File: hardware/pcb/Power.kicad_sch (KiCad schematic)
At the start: 17 parts, among them J4 USB_B_Micro, SW2 CSS-1210TB, U3 MCP73831-2-OT, U4 TL431DBZ, U5 TLV73333PDBV

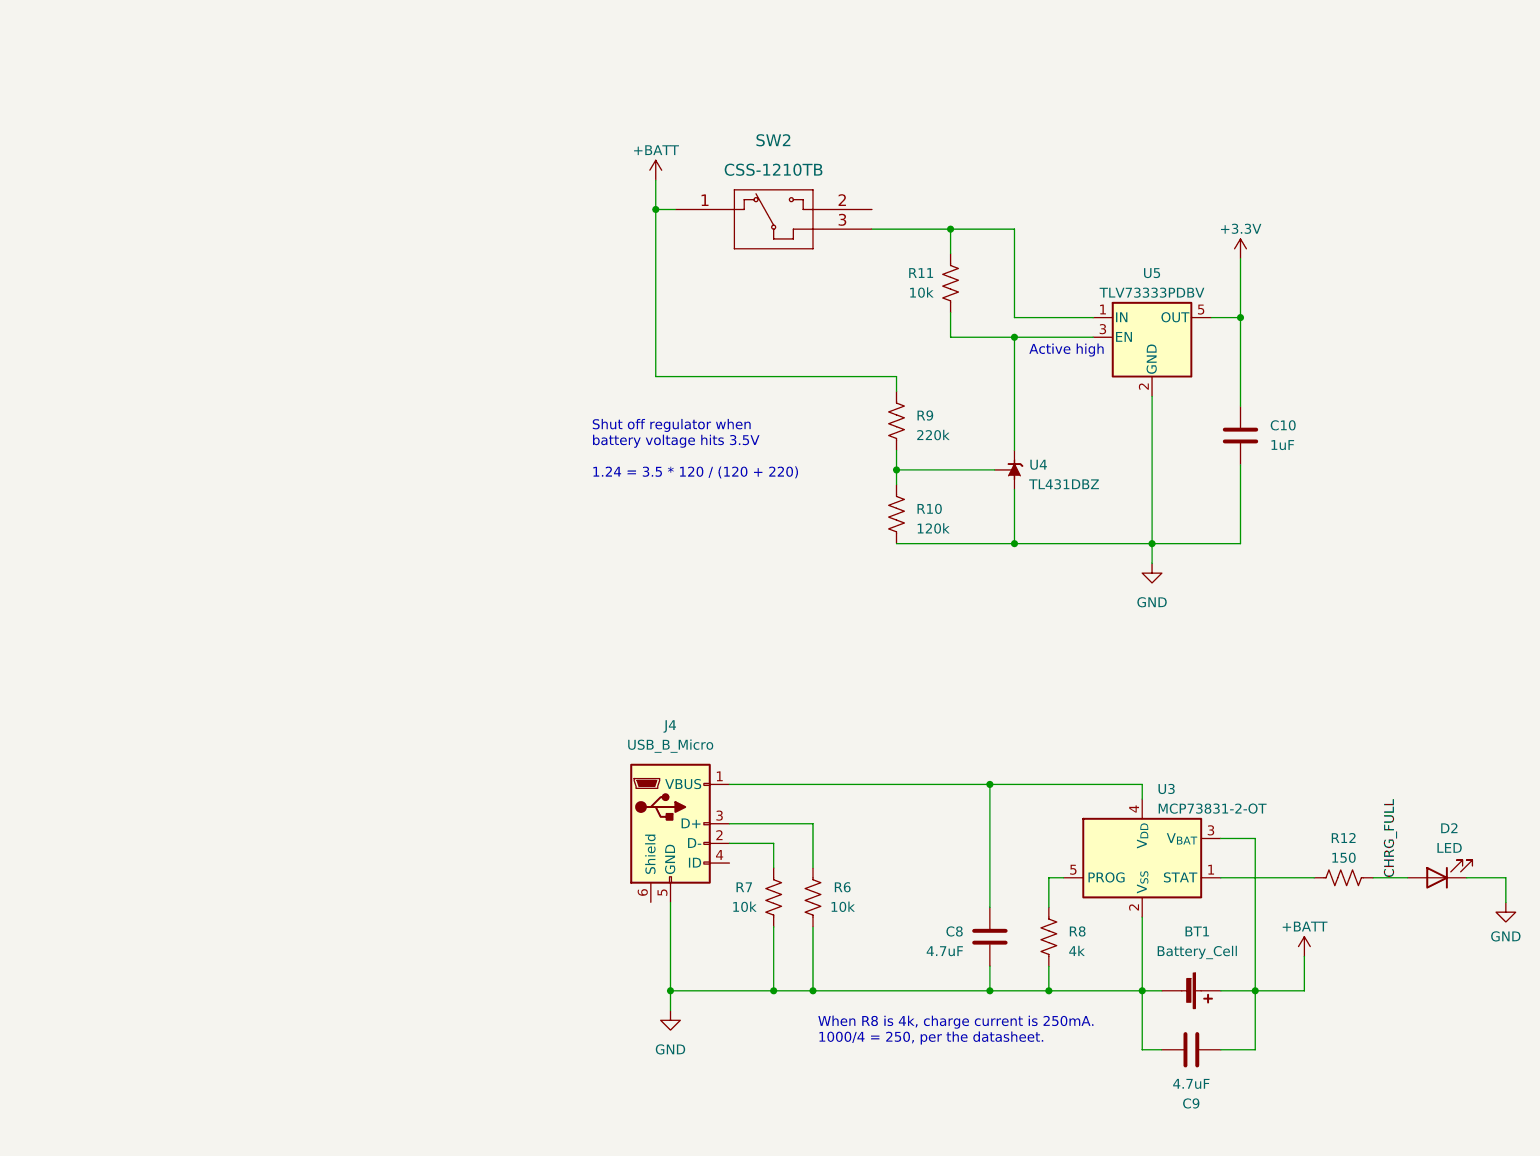
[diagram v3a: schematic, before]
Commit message: Update PCB from updated schematic
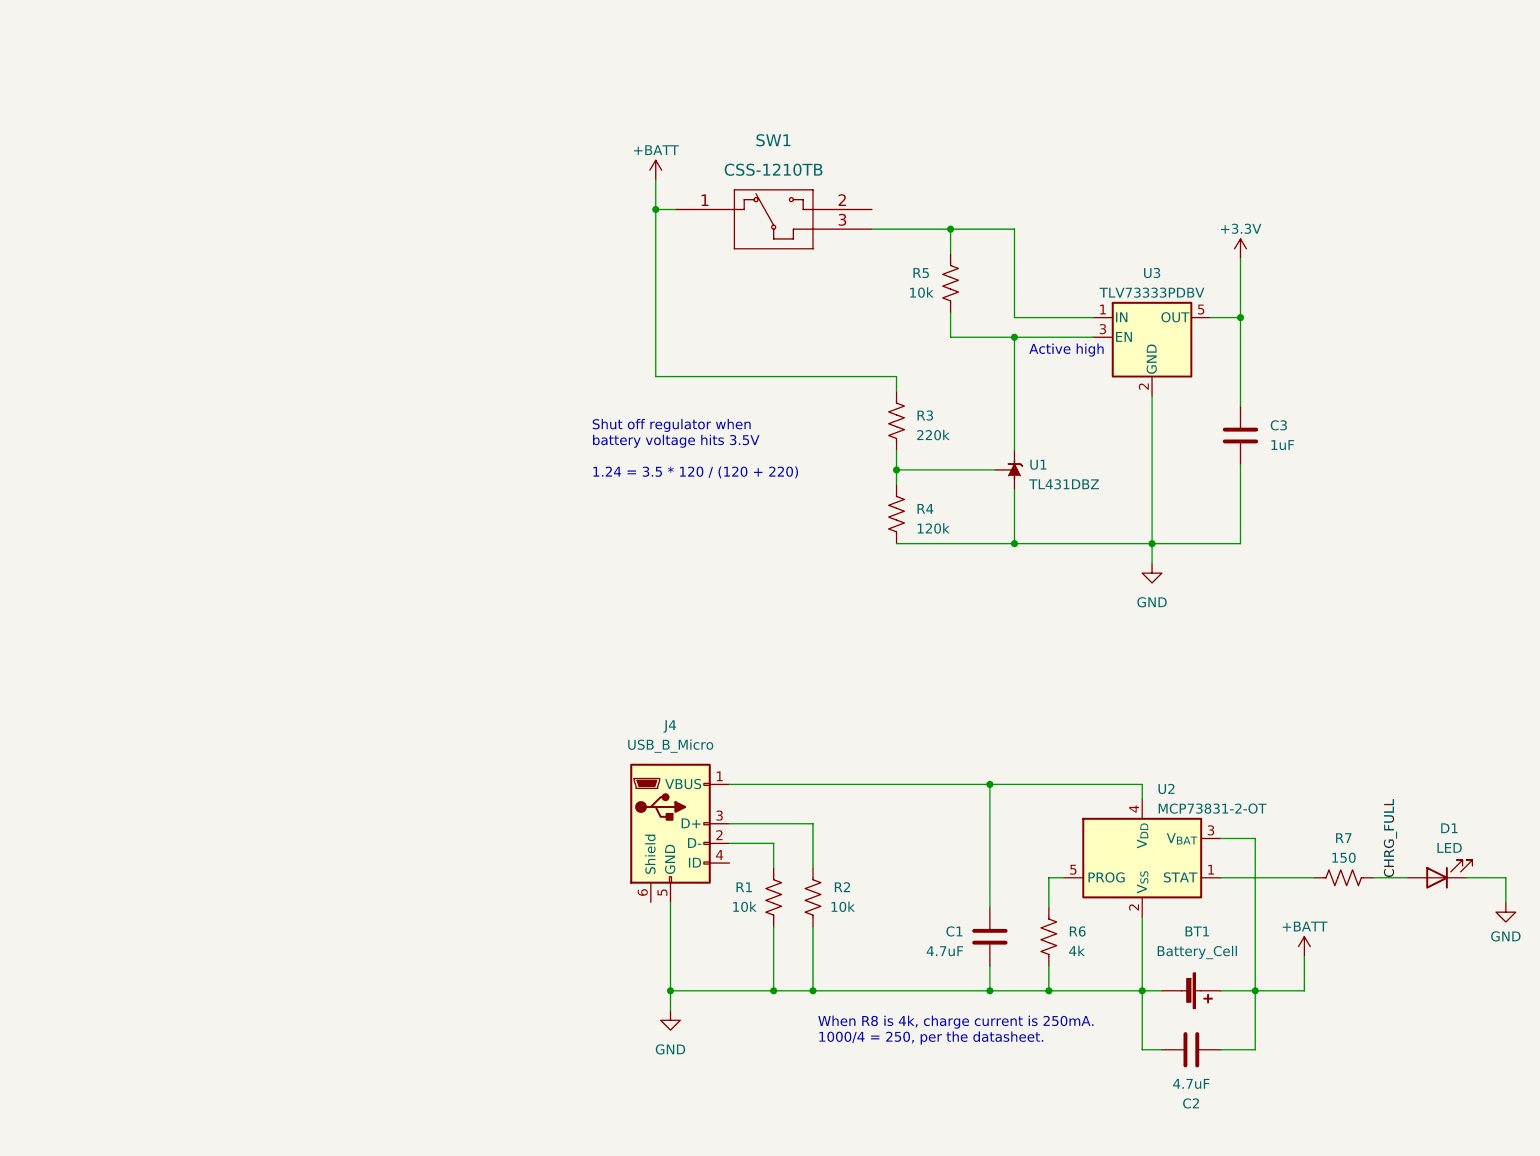
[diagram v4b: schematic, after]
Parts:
- renumbered C8 to C1, C9 to C2, C10 to C3, D2 to D1, R7 to R1, R6 to R2, R9 to R3, R10 to R4, R11 to R5, R8 to R6, R12 to R7, SW2 to SW1, U4 to U1, U3 to U2, U5 to U3

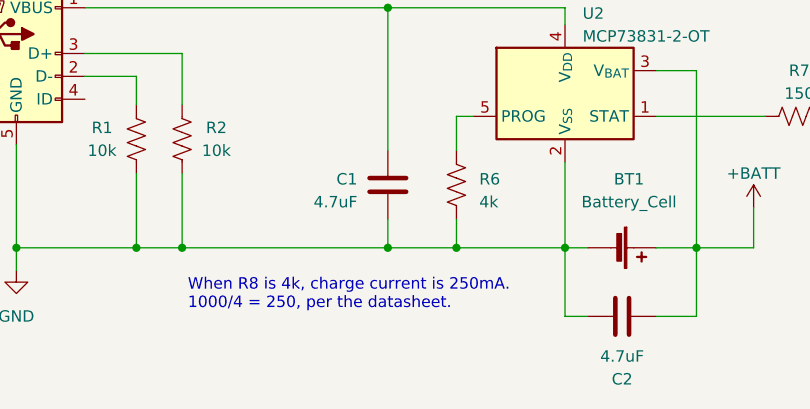
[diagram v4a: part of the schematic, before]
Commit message: Replace third party MAX98357 symbol with custom one
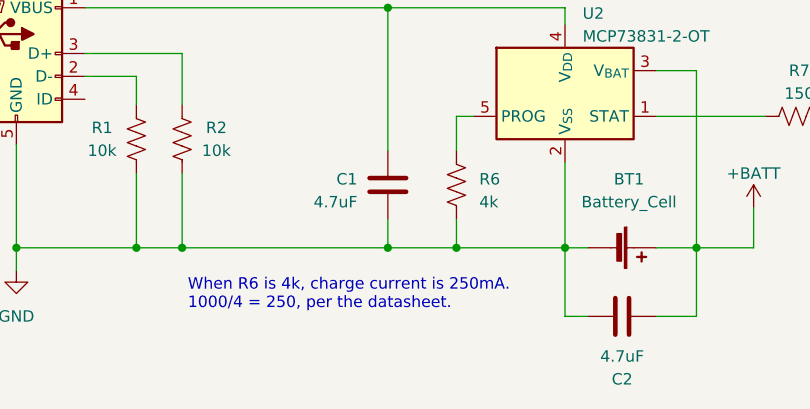
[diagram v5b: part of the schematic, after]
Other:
- note added: "When R6 is 4k, charge current is 250mA. 1000/4 = 250, per the datasheet."
- note removed: "When R8 is 4k, charge current is 250mA. 1000/4 = 250, per the datasheet."
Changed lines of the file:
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@@
     (effects (font (size 1.27 1.27)) (justify left bottom))
   )
-  (text "When R8 is 4k, charge current is 250mA.\n1000/4 = 250, per the datasheet."
+  (text "When R6 is 4k, charge current is 250mA.\n1000/4 = 250, per the datasheet."
     (at 121.285 146.685 0)
     (effects (font (size 1.27 1.27)) (justify left bottom))

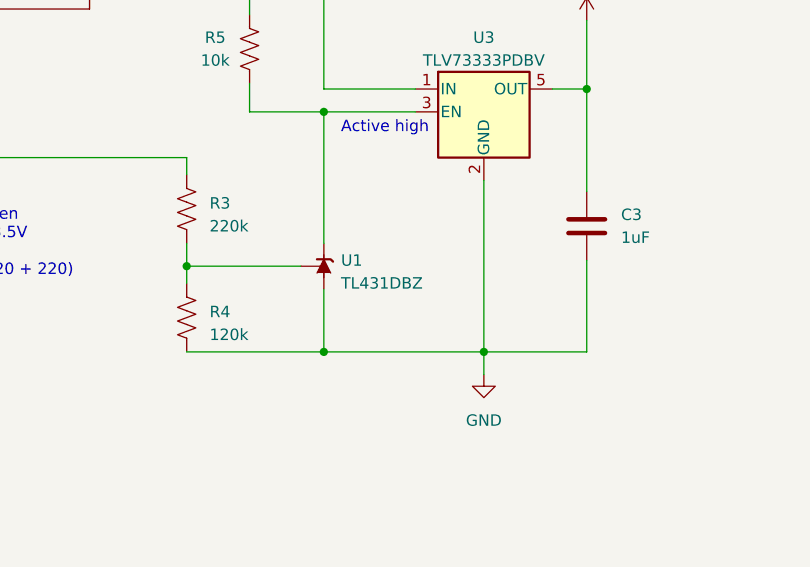
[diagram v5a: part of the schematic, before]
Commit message: Replace stand-in symbol with custom one for TLV431
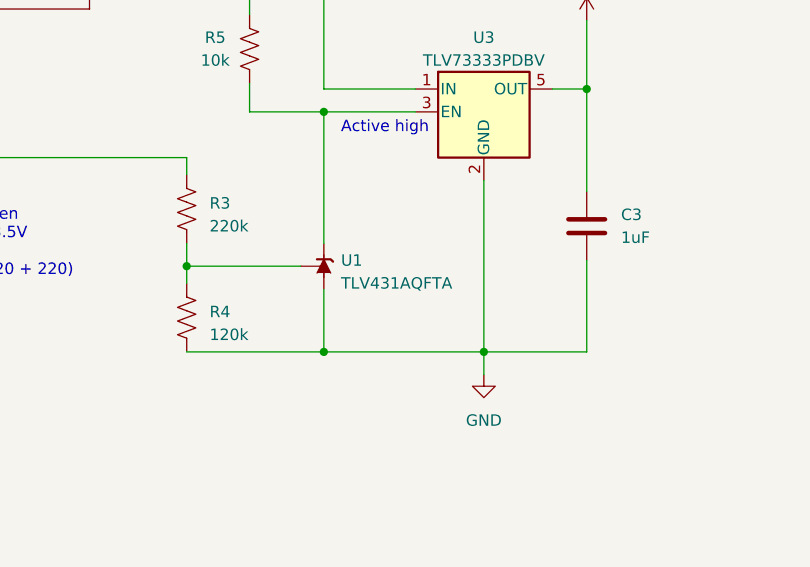
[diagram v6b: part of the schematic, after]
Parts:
- removed U1: TL431DBZ, Package_TO_SOT_SMD:SOT-23, symbol Reference_Voltage:TL431DBZ
- added U1: TLV431AQFTA, Package_TO_SOT_SMD:SOT-23, symbol TLV431Q:TLV431AQFTA
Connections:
- net GND: now also U1.3 (A)
- net at R3.1, R4.2: now also U1.1 (REF)
- net at R5.2, U3.3 (EN): now also U1.2 (K)
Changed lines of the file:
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@@
-    )
-  )
-  (symbol (lib_id "Reference_Voltage:TL431DBZ") (at 146.685 72.39 90) (unit 1)
-    (in_bom yes) (on_board yes) (dnp no) (fields_autoplaced)
-    (property "Reference" "U1" (at 148.59 71.755 90)
-      (effects (font (size 1.27 1.27)) (justify right))
-    )
-    (property "Value" "TL431DBZ" (at 148.59 74.295 90)
-      (effects (font (size 1.27 1.27)) (justify right))
-    )
-    (property "Footprint" "Package_TO_SOT_SMD:SOT-23" (at 150.495 72.39 0)
-      (effects (font (size 1.27 1.27) italic) hide)
-    )
-    (property "Datasheet" "http://www.ti.com/lit/ds/symlink/tl431.pdf" (at 146.685 72.39 0)
-      (effects (font (size 1.27 1.27) italic) hide)
-    )
-    (pin "1")
-    (pin "2")
-    (pin "3")
-    (instances
-      (project "Combadge"
-        (path "/dc42e7bc-f663-434d-8744-232038ac4fdf/522738f4-f6b2-4897-a079-07da122bd152"
-          (reference "U1") (unit 1)
-        )
-      )
     )
   )
@@
         )
       )
+    )
+  )
+  (symbol (lib_id "TLV431Q:TLV431AQFTA") (at 146.685 72.39 90) (unit 1)
+    (in_bom yes) (on_board yes) (dnp no) (fields_autoplaced)
+    (property "Reference" "U1" (at 148.59 71.755 90)
+      (effects (font (size 1.27 1.27)) (justify right))
+    )
+    (property "Value" "TLV431AQFTA" (at 148.59 74.295 90)
+      (effects (font (size 1.27 1.27)) (justify right))
+    )
+    (property "Footprint" "Package_TO_SOT_SMD:SOT-23" (at 144.145 71.12 0)
+      (effects (font (size 1.27 1.27)) hide)
+    )
+    (property "Datasheet" "https://www.diodes.com/assets/Datasheets/TLV431Q.pdf" (at 144.145 71.12 0)
+      (effects (font (size 1.27 1.27)) hide)
+    )
+    (pin "1")
+    (pin "2")
+    (pin "3")
+    (instances
+      (project "Combadge"
+        (path "/dc42e7bc-f663-434d-8744-232038ac4fdf/522738f4-f6b2-4897-a079-07da122bd152"
+          (reference "U1") (unit 1)
+        )
+      )

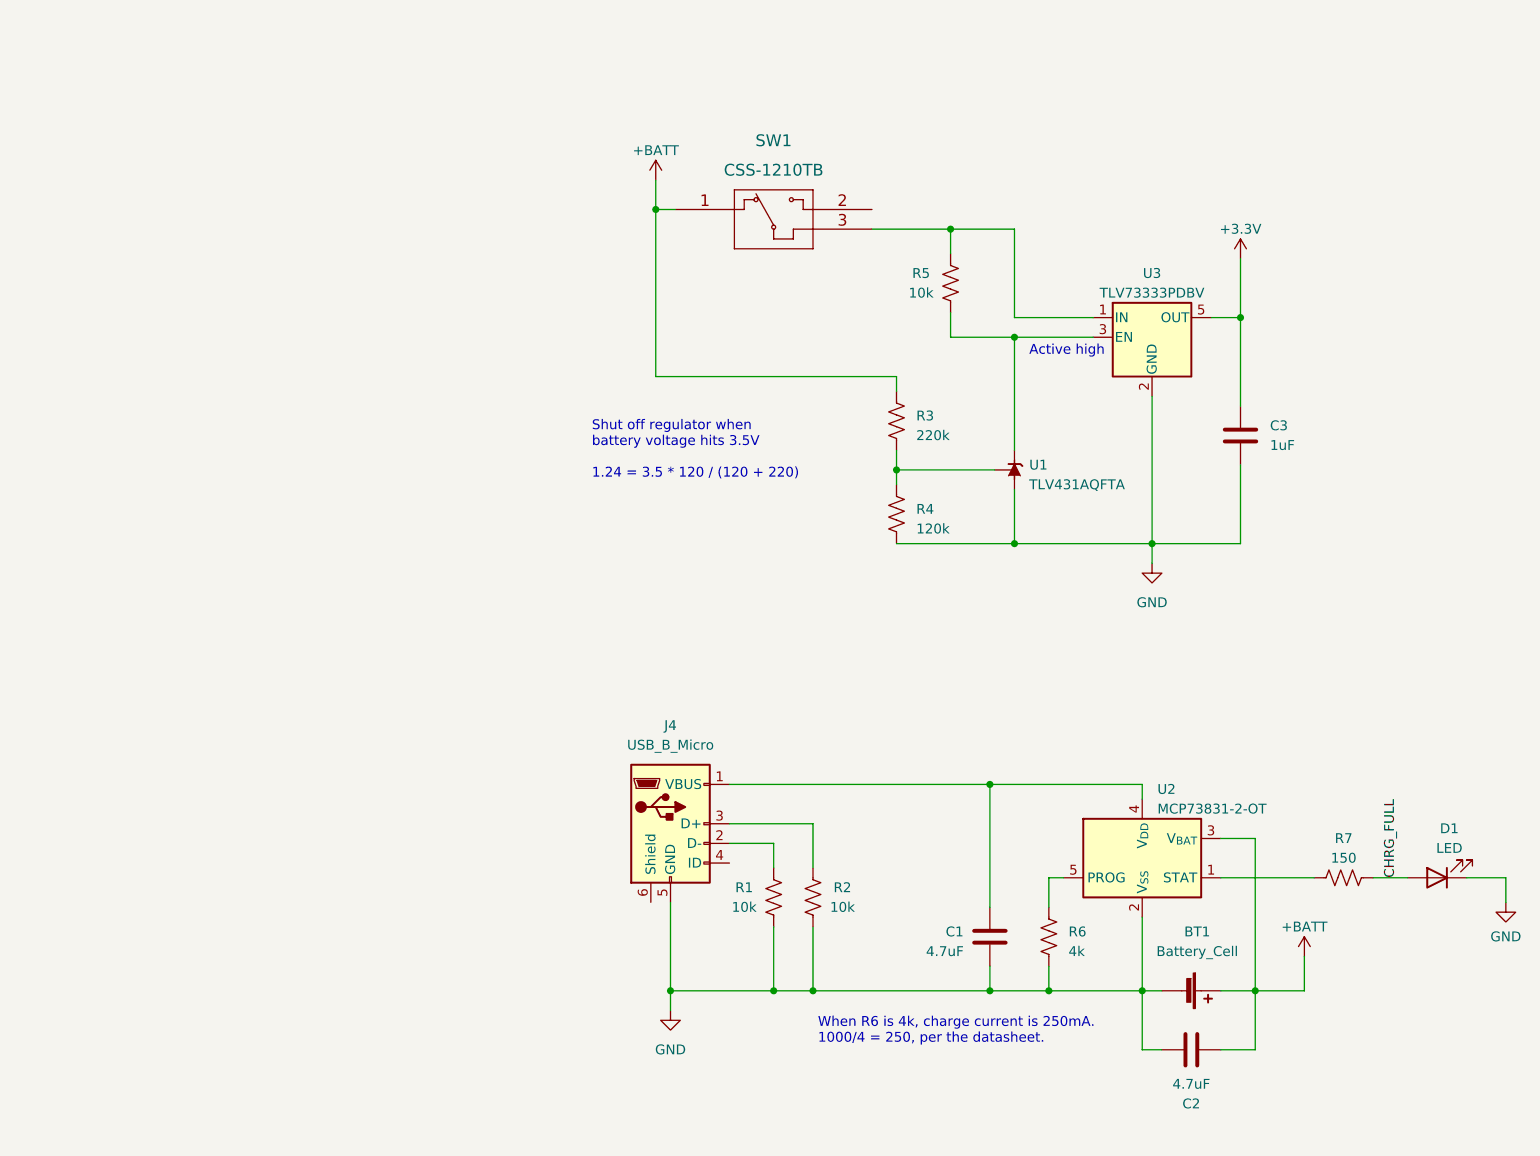
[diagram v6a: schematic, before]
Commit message: Replace ESP32 with ESP32-S3
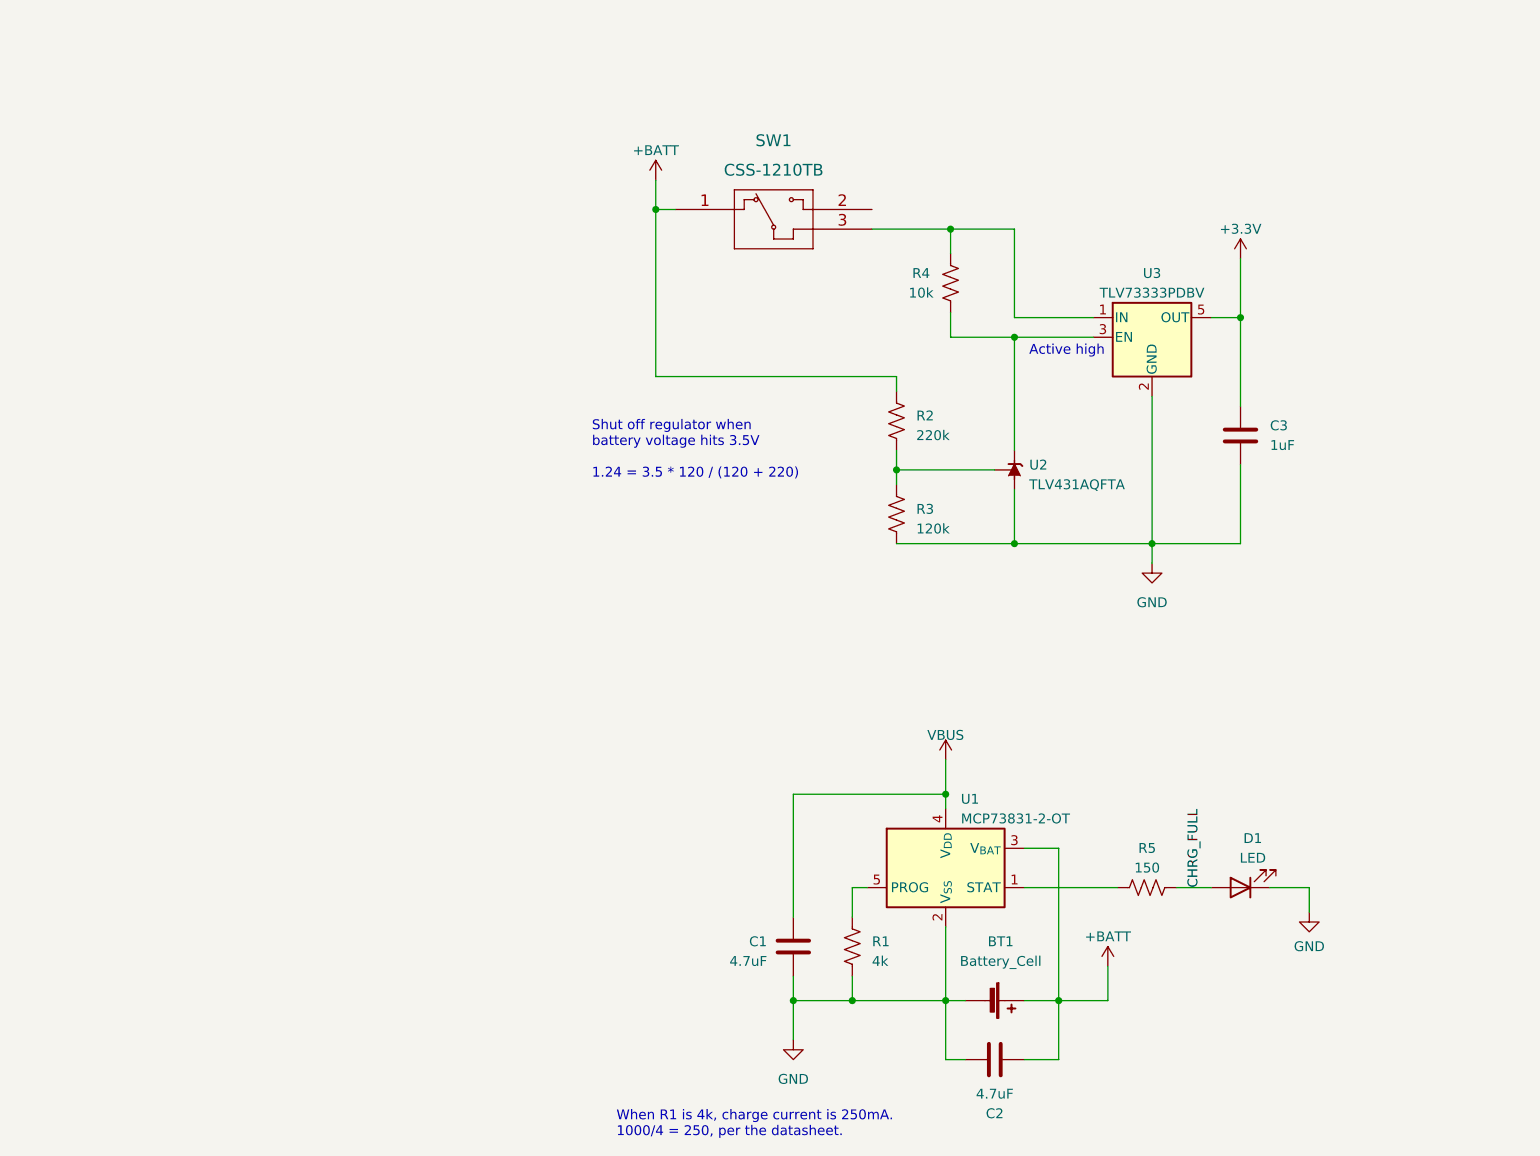
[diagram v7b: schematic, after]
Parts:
- removed J4: USB_B_Micro, Connector_USB:USB_Micro-B_Amphenol_10118194_Horizontal, symbol Connector:USB_B_Micro
- removed R1, R2: 10k, Resistor_SMD:R_1206_3216Metric_Pad1.30x1.75mm_HandSolder, symbol Device:R_US
- renumbered R6 to R1, R3 to R2, R4 to R3, R5 to R4, R7 to R5, U2 to U1, U1 to U2
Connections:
- net VBUS: now reaches C1.1, U1.4 (V_{DD})
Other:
- note added: "When R1 is 4k, charge current is 250mA. 1000/4 = 250, per the datasheet."
- note removed: "When R6 is 4k, charge current is 250mA. 1000/4 = 250, per the datasheet."
- moved on the sheet: BT1, C1, C2, D1, R1, R5, U1

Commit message: Miscellaneous cleanup
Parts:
- BT1: now left out of the parts list
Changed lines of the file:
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@@
   )
   (symbol (lib_id "Device:Battery_Cell") (at 142.875 140.97 270) (unit 1)
-    (in_bom yes) (on_board yes) (dnp no) (fields_autoplaced)
+    (in_bom no) (on_board yes) (dnp no) (fields_autoplaced)
     (property "Reference" "BT1" (at 144.907 133.35 90)
       (effects (font (size 1.27 1.27)))
